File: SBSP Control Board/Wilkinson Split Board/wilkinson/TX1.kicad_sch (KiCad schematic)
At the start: 13 parts, among them U4 ADAR1000ACCZN

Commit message: fixed routing
monday: 5 hrs: talked to fayed about what exactly we needed to do, emailed fathy about what we do, get approval, re do schematic and layout to get wilkinson layout started. started workin on new schematic, started creating the adar1000 footprint and sch symbol, re did board outline and got traces from xmicrowave board, started doing layout for adar supporting passive components.

tuesday, 3 hrs (12-3), worked on adding level shifting circuit and began designing schematic for level shifting and ensuring each power level was correct and the schematic was equal in function to the evaluation board schematic.

wednesday: 5 (10-3), further schematic work, finished schematic, and then began layout for board. got wilkinson geometry from fayed and began its implementation into the design. layout is not done yet, but should not take much longer.

thursday: 5 (10-3)more layout work on the schematic, finished the level shifting circuit and added the power side to the layout and circuit.
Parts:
- renumbered R22 to R28
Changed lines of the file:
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@@
 		(dnp no)
 		(fields_autoplaced yes)
-		(property "Reference" "#PWR037"
+		(property "Reference" "#PWR038"
 			(at 129.54 144.78 0)
 			(hide yes)
@@
 			(project "trace_pretty"
 				(path "/76e8d6dc-1e9d-412e-b6a2-7cc6673d2c89/b4db71ec-ce9e-44fa-8ec8-a087008386f2"
-					(reference "#PWR037")
+					(reference "#PWR038")
 					(unit 1)
 				)
@@
 		(dnp no)
 		(fields_autoplaced yes)
-		(property "Reference" "#PWR035"
+		(property "Reference" "#PWR036"
 			(at 114.3 67.31 0)
 			(hide yes)
@@
 			(project "trace_pretty"
 				(path "/76e8d6dc-1e9d-412e-b6a2-7cc6673d2c89/b4db71ec-ce9e-44fa-8ec8-a087008386f2"
-					(reference "#PWR035")
+					(reference "#PWR036")
 					(unit 1)
 				)
@@
 		(dnp no)
 		(fields_autoplaced yes)
-		(property "Reference" "#PWR036"
+		(property "Reference" "#PWR037"
 			(at 124.46 64.77 0)
 			(hide yes)
@@
 			(project "trace_pretty"
 				(path "/76e8d6dc-1e9d-412e-b6a2-7cc6673d2c89/b4db71ec-ce9e-44fa-8ec8-a087008386f2"
-					(reference "#PWR036")
+					(reference "#PWR037")
 					(unit 1)
 				)
@@
 		(dnp no)
 		(fields_autoplaced yes)
-		(property "Reference" "#PWR034"
+		(property "Reference" "#PWR035"
 			(at 107.95 195.58 0)
 			(hide yes)
@@
 			(project "trace_pretty"
 				(path "/76e8d6dc-1e9d-412e-b6a2-7cc6673d2c89/b4db71ec-ce9e-44fa-8ec8-a087008386f2"
-					(reference "#PWR034")
+					(reference "#PWR035")
 					(unit 1)
 				)
@@
 		(dnp no)
 		(fields_autoplaced yes)
-		(property "Reference" "#PWR032"
+		(property "Reference" "#PWR033"
 			(at 87.63 145.415 0)
 			(hide yes)
@@
 			(project "trace_pretty"
 				(path "/76e8d6dc-1e9d-412e-b6a2-7cc6673d2c89/b4db71ec-ce9e-44fa-8ec8-a087008386f2"
-					(reference "#PWR032")
+					(reference "#PWR033")
 					(unit 1)
 				)
@@
 		(dnp no)
 		(fields_autoplaced yes)
-		(property "Reference" "#PWR041"
+		(property "Reference" "#PWR042"
 			(at 270.51 255.27 0)
 			(hide yes)
@@
 			(project "trace_pretty"
 				(path "/76e8d6dc-1e9d-412e-b6a2-7cc6673d2c89/b4db71ec-ce9e-44fa-8ec8-a087008386f2"
-					(reference "#PWR041")
+					(reference "#PWR042")
 					(unit 1)
 				)
@@
 		(dnp no)
 		(fields_autoplaced yes)
-		(property "Reference" "#PWR033"
+		(property "Reference" "#PWR034"
 			(at 101.6 95.25 0)
 			(hide yes)
@@
 			(project "trace_pretty"
 				(path "/76e8d6dc-1e9d-412e-b6a2-7cc6673d2c89/b4db71ec-ce9e-44fa-8ec8-a087008386f2"
-					(reference "#PWR033")
+					(reference "#PWR034")
 					(unit 1)
 				)
@@
 		(dnp no)
 		(fields_autoplaced yes)
-		(property "Reference" "#PWR039"
+		(property "Reference" "#PWR040"
 			(at 160.02 195.58 0)
 			(hide yes)
@@
 			(project "trace_pretty"
 				(path "/76e8d6dc-1e9d-412e-b6a2-7cc6673d2c89/b4db71ec-ce9e-44fa-8ec8-a087008386f2"
-					(reference "#PWR039")
+					(reference "#PWR040")
 					(unit 1)
 				)
@@
 		(dnp no)
 		(fields_autoplaced yes)
-		(property "Reference" "#PWR031"
+		(property "Reference" "#PWR032"
 			(at 67.945 160.02 0)
 			(hide yes)
@@
 			(project "trace_pretty"
 				(path "/76e8d6dc-1e9d-412e-b6a2-7cc6673d2c89/b4db71ec-ce9e-44fa-8ec8-a087008386f2"
-					(reference "#PWR031")
+					(reference "#PWR032")
 					(unit 1)
 				)
@@
 		(dnp no)
 		(fields_autoplaced yes)
-		(property "Reference" "R22"
+		(property "Reference" "R28"
 			(at 115.57 88.9 90)
 			(show_name no)
@@
 			(project "trace_pretty"
 				(path "/76e8d6dc-1e9d-412e-b6a2-7cc6673d2c89/b4db71ec-ce9e-44fa-8ec8-a087008386f2"
-					(reference "R22")
+					(reference "R28")
 					(unit 1)
 				)
@@
 		(dnp no)
 		(fields_autoplaced yes)
-		(property "Reference" "#PWR038"
+		(property "Reference" "#PWR039"
 			(at 134.62 195.58 0)
 			(hide yes)
@@
 			(project "trace_pretty"
 				(path "/76e8d6dc-1e9d-412e-b6a2-7cc6673d2c89/b4db71ec-ce9e-44fa-8ec8-a087008386f2"
-					(reference "#PWR038")
+					(reference "#PWR039")
 					(unit 1)
 				)
@@
 		(dnp no)
 		(fields_autoplaced yes)
-		(property "Reference" "#PWR040"
+		(property "Reference" "#PWR041"
 			(at 186.69 195.58 0)
 			(hide yes)
@@
 			(project "trace_pretty"
 				(path "/76e8d6dc-1e9d-412e-b6a2-7cc6673d2c89/b4db71ec-ce9e-44fa-8ec8-a087008386f2"
-					(reference "#PWR040")
+					(reference "#PWR041")
 					(unit 1)
 				)

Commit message: added wilkinson geometry
11:00 to 3:00

learned from nolan how the thing works and how to run and use it/test it. I then worked on the control circuit testing and wrote report on it. individually tested every patch to ensure the values matched the MATLAB sims. this took about 2 hours. the next two hours was spent working on the 1-8 splitter board. I finished adding the wilkinson geometry onto the board and began laying out the passive components.
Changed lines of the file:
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@@
-		)
-	)
-	(label "PLL_IN"
-		(at 124.46 125.73 180)
-		(effects
-			(font
-				(size 1.27 1.27)
-			)
-			(justify right bottom)
 		)
 	)
@@
 			)
 		)
+	)
+	(global_label "PLL_IN"
+		(shape input)
+		(at 124.46 125.73 180)
+		(fields_autoplaced yes)
+		(effects
+			(font
+				(size 1.27 1.27)
+			)
+			(justify right)
+		)
+		(property "Intersheetrefs" "${INTERSHEET_REFS}"
+			(at 115.2457 125.73 0)
+			(hide yes)
+			(show_name no)
+			(do_not_autoplace no)
+			(effects
+				(font
+					(size 1.27 1.27)
+				)
+				(justify right)
+			)
+		)

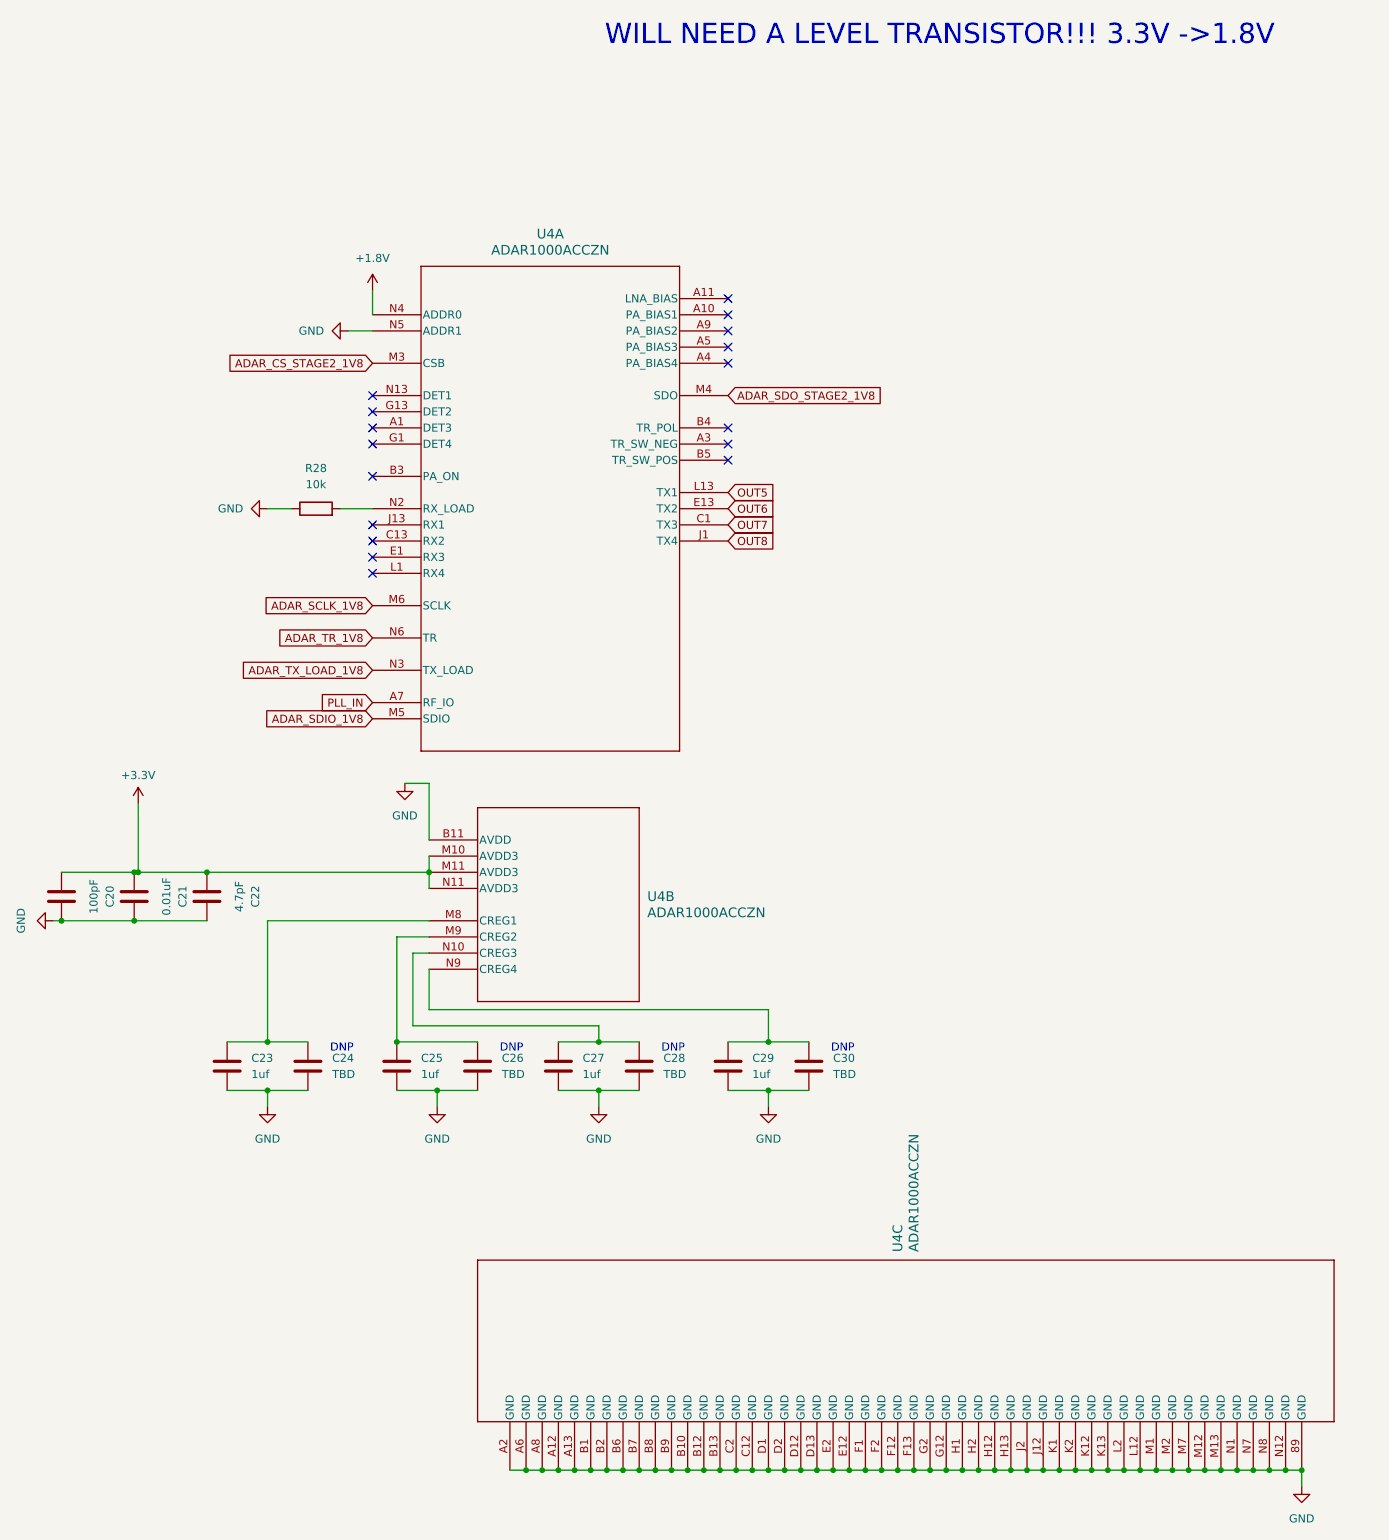
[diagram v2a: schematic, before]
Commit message: finished schematic and routing rev1
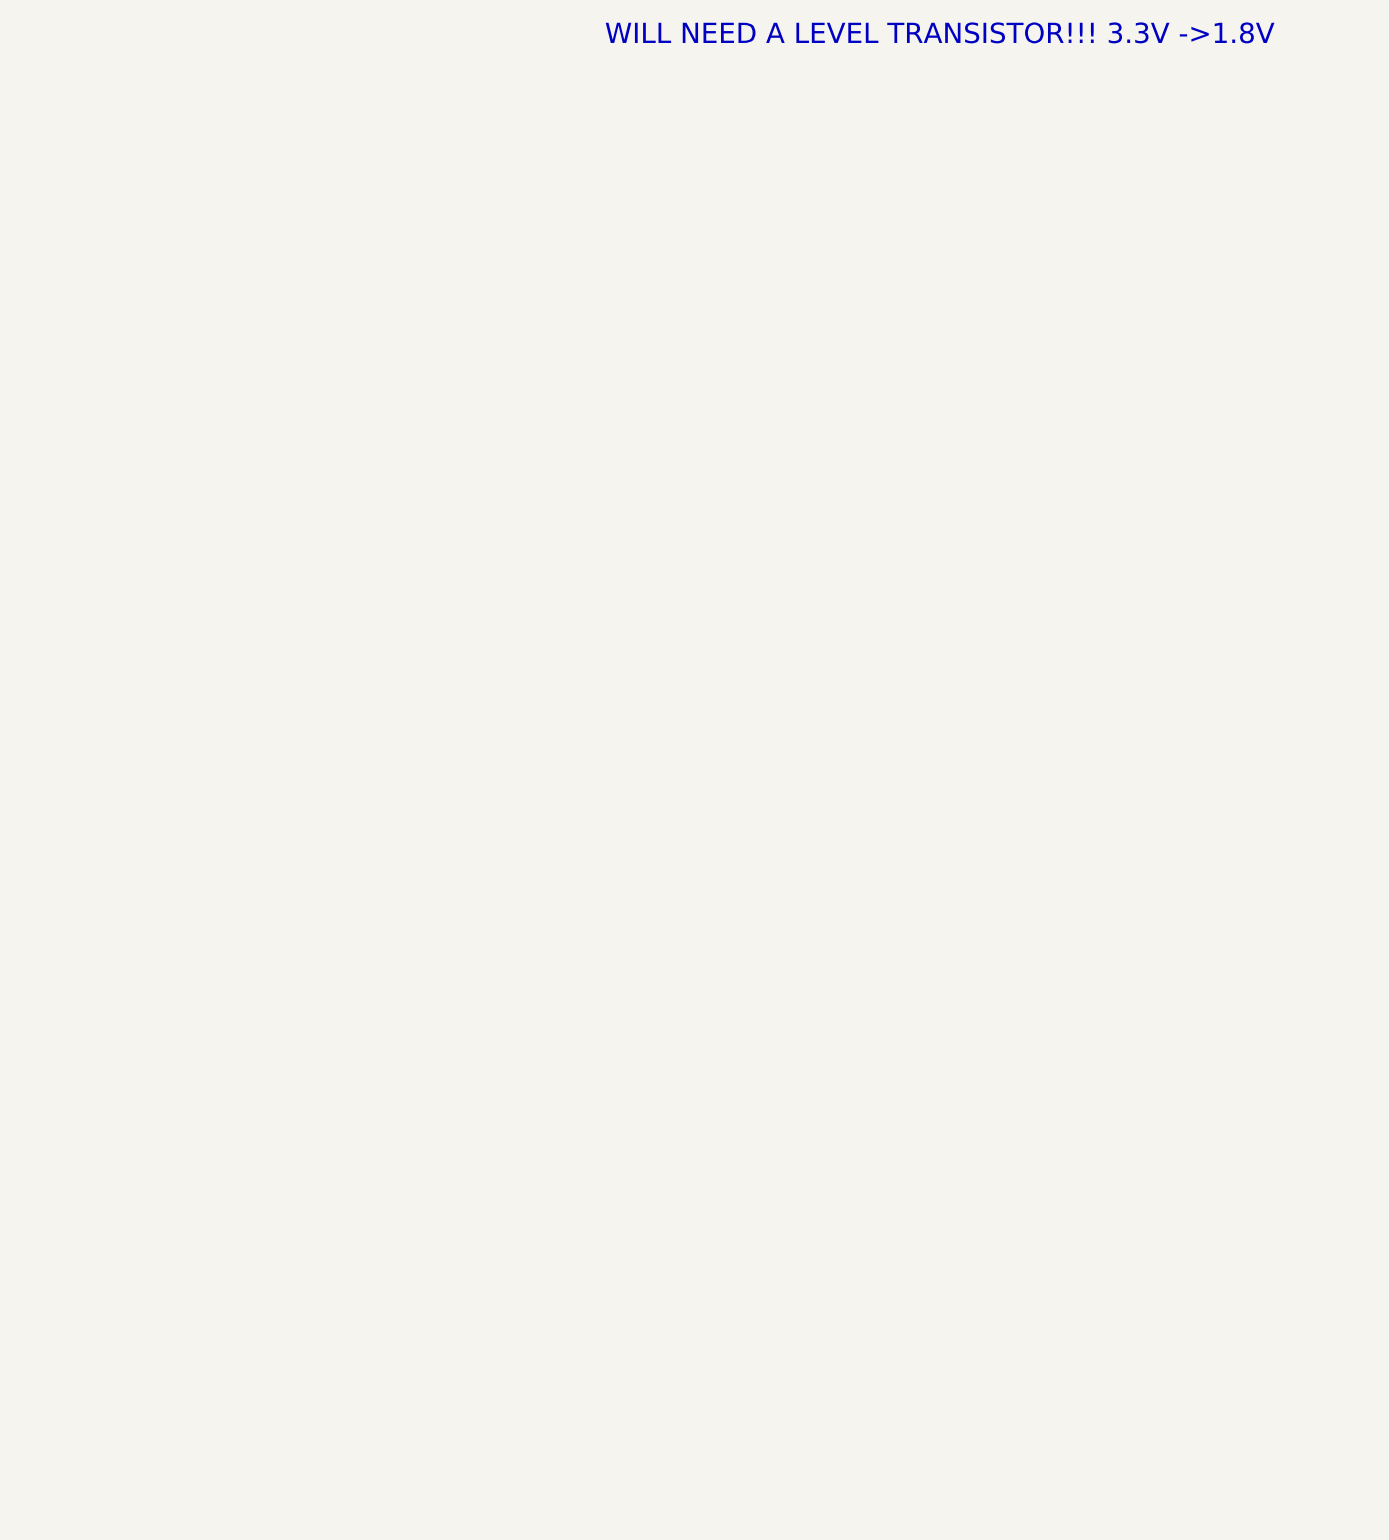
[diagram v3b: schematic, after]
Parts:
- removed C20: 100pF, Resistor_SMD:R_0603_1608Metric, symbol Device:C
- removed C21: 0.01uF, Resistor_SMD:R_0603_1608Metric, symbol Device:C
- removed C22: 4.7pF, Resistor_SMD:R_0603_1608Metric, symbol Device:C
- removed C23, C25, C27, C29: 1uf, Resistor_SMD:R_0603_1608Metric, symbol Device:C
- removed C24, C26, C28, C30: TBD, Resistor_SMD:R_0603_1608Metric, symbol Device:C
- removed R28: 10k, Resistor_SMD:R_0603_1608Metric, symbol Device:R
- removed U4: ADAR1000ACCZN, adar1000:CC-88-1_ADI, symbol ADAR1000:ADAR1000ACCZN
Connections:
- no-connect marks 17 -> 0
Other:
- note removed: "DNP"
